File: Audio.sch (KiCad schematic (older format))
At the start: 35 parts, among them J1 AUDIO JACK, J2 AUDIO JACK, J3 AUDIO JACK, J4 AUDIO JACK, U10 TLV320AIC3104

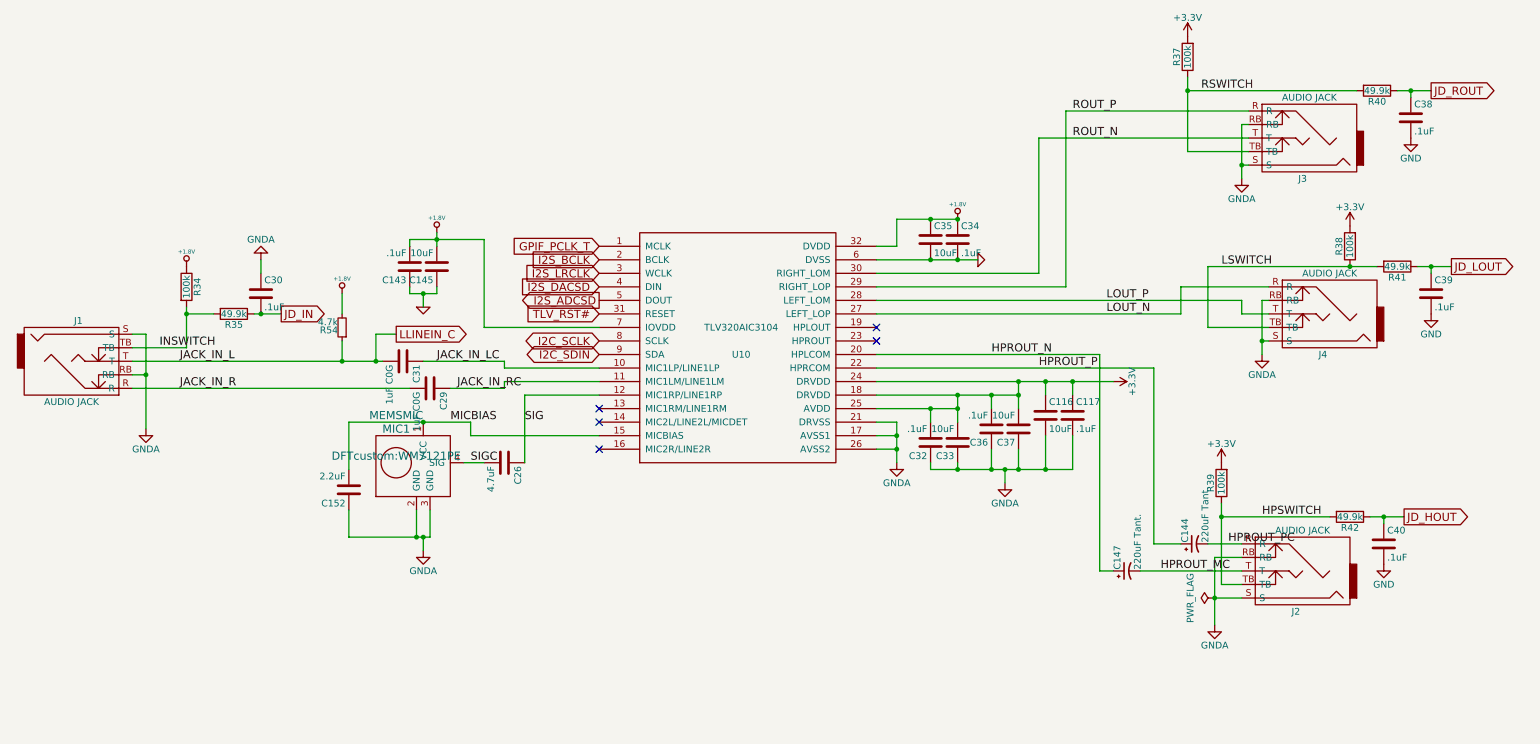
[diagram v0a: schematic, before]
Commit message: encoders and headphone jack have been modified. many unconnections
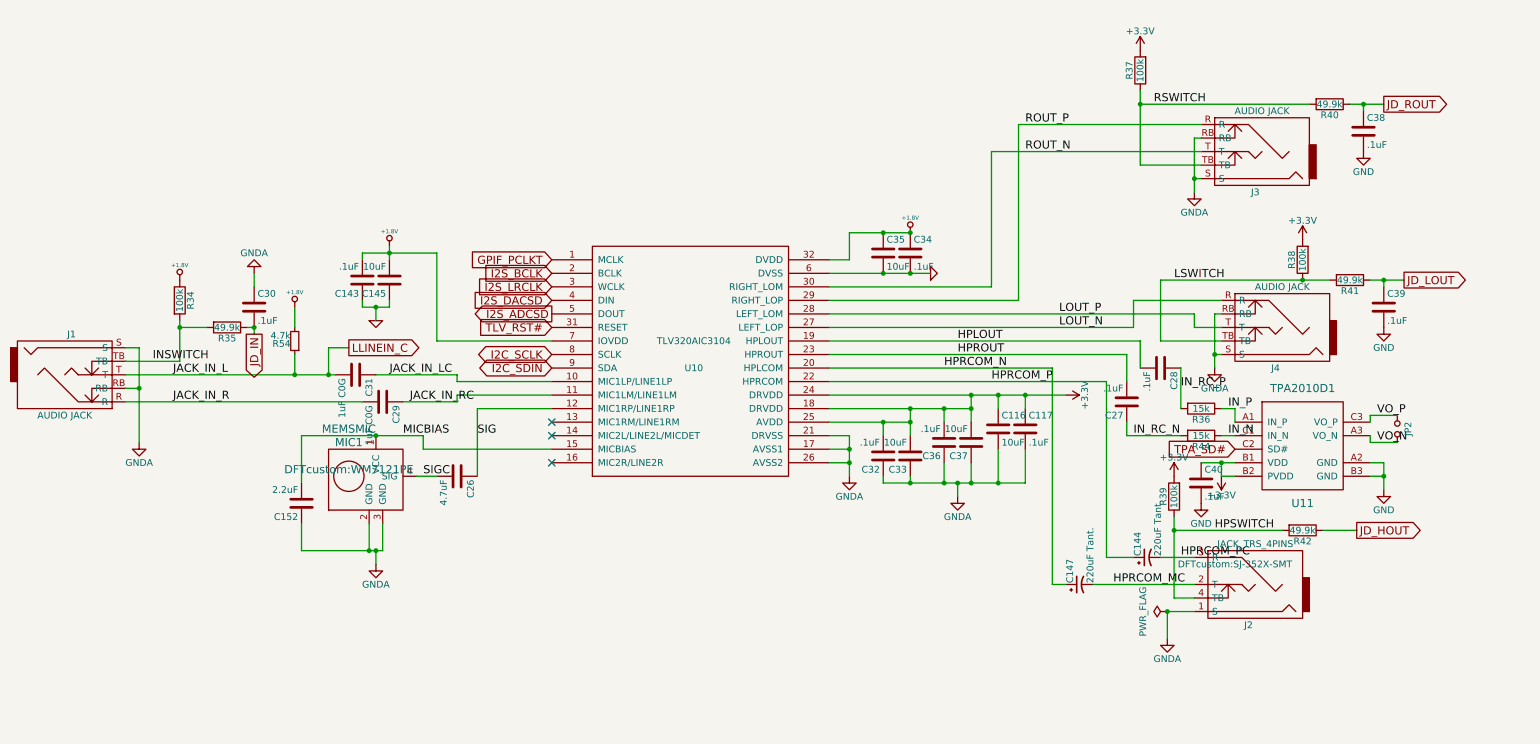
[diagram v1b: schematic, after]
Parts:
- removed J2: AUDIO JACK, DFTcustom:RA49C14B, symbol JACK_TRS_5PINS
- added C27, C28: .1uF, Capacitors_SMD:C_0603, symbol C
- added J2: JACK_TRS_4PINS, DFTcustom:SJ-352X-SMT, symbol JACK_TRS_4PINS
- added JP2: Jumper_NO_Small, DFTcustom:JUMPER_2PIN, symbol Jumper_NO_Small
- added R36, R44: 15k, Resistors_SMD:R_0402, symbol R
- added U11: TPA2010D1, DFTcustom:9DSBGA, symbol TPA2010D1
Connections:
- net +3V3: now also C40.1, U11.B1 (VDD), U11.B2 (PVDD)
- net GND: now also U11.A2 (GND), U11.B3 (GND)
- net GNDA: now also J2.1 (S)
- net HPSWITCH: now also J2.4 (TB)
- net JD_HOUT: no longer C40.1
- net HPLOUT: now reaches U10.19 (HPLOUT)
- net HPLOUT: now also C28.2
- net HPROUT: now reaches U10.23 (HPROUT)
- net HPROUT: now also C27.2
- net GPIF_PCLK_T renamed GPIF_PCLKT
- net HPROUT_MC renamed HPRCOM_MC
- net HPRCOM_MC: now also J2.2 (T)
- net HPROUT_N renamed HPRCOM_N
- net HPROUT_P renamed HPRCOM_P
- net HPROUT_PC renamed HPRCOM_PC
- net HPRCOM_PC: now also J2.3 (R)
- new net IN_N: R44.1, U11.C1 (IN_N)
- new net IN_P: R36.1, U11.A1 (IN_P)
- new net IN_RC_N: C27.1, R44.2
- new net IN_RC_P: C28.1, R36.2
- new net TPA_SD#: U11.C2 (SD#)
- new net VO_N: JP2.2, U11.A3 (VO_N)
- new net VO_P: JP2.1, U11.C3 (VO_P)
- no-connect marks 5 -> 3
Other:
- moved on the sheet: C116, C117, C143, C144, C145, C147, C152, C26, C29, C30, C31, C32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

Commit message: screen attached!
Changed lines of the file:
@@
 $Descr A4 11693 8268
 encoding utf-8
-Sheet 8 15
+Sheet 8 14
 Title ""
 Date ""
@@
 Text GLabel 4600 3300 0    60   Input ~ 0
 I2S_BCLK
-Text GLabel 4600 3600 0    60   Output ~ 0
+Text GLabel 4600 3600 0    60   BiDi ~ 0
 I2S_ADCSD
 Text GLabel 4600 3500 0    60   Input ~ 0
@@
 $EndComp
 $Comp
-L GND #PWR078
+L GND #PWR071
 U 1 1 5863064B
 P 10600 2400
-F 0 "#PWR078" H 10600 2150 50  0001 C CNN
+F 0 "#PWR071" H 10600 2150 50  0001 C CNN
 F 1 "GND" H 10600 2250 50  0000 C CNN
 F 2 "" H 10600 2400 50  0000 C CNN
@@
 $EndComp
 $Comp
-L GND #PWR079
+L GND #PWR072
 U 1 1 58630693
 P 10750 3700
-F 0 "#PWR079" H 10750 3450 50  0001 C CNN
+F 0 "#PWR072" H 10750 3450 50  0001 C CNN
 F 1 "GND" H 10750 3550 50  0000 C CNN
 F 2 "" H 10750 3700 50  0000 C CNN
@@
 $EndComp
 $Comp
-L GND #PWR080
+L GND #PWR073
 U 1 1 586306DB
 P 9400 5000
-F 0 "#PWR080" H 9400 4750 50  0001 C CNN
+F 0 "#PWR073" H 9400 4750 50  0001 C CNN
 F 1 "GND" H 9400 4850 50  0000 C CNN
 F 2 "" H 9400 5000 50  0000 C CNN
@@
 JD_HOUT
 $Comp
-L +1.8V #PWR081
+L +1.8V #PWR074
 U 1 1 58631585
 P 1850 3350
-F 0 "#PWR081" H 1850 3490 20  0001 C CNN
+F 0 "#PWR074" H 1850 3490 20  0001 C CNN
 F 1 "+1.8V" H 1850 3460 30  0000 C CNN
 F 2 "" H 1850 3350 60  0001 C CNN
@@
 JD_IN
 $Comp
-L +3.3V #PWR082
+L +3.3V #PWR075
 U 1 1 5874382A
 P 8950 1650
-F 0 "#PWR082" H 8950 1500 50  0001 C CNN
+F 0 "#PWR075" H 8950 1500 50  0001 C CNN
 F 1 "+3.3V" H 8950 1790 50  0000 C CNN
 F 2 "" H 8950 1650 50  0000 C CNN
@@
 	1550 3850 1550 4550
 $Comp
-L GNDA #PWR083
+L GNDA #PWR076
 U 1 1 58783406
 P 1550 4550
-F 0 "#PWR083" H 1550 4300 50  0001 C CNN
+F 0 "#PWR076" H 1550 4300 50  0001 C CNN
 F 1 "GNDA" H 1550 4400 50  0000 C CNN
 F 2 "" H 1550 4550 50  0000 C CNN
@@
 SIGC
 $Comp
-L GNDA #PWR084
+L GNDA #PWR077
 U 1 1 588330FF
 P 9150 6000
-F 0 "#PWR084" H 9150 5750 50  0001 C CNN
+F 0 "#PWR077" H 9150 5750 50  0001 C CNN
 F 1 "GNDA" H 9150 5850 50  0000 C CNN
 F 2 "" H 9150 6000 50  0000 C CNN
@@
 	2400 3400 2400 3300
 $Comp
-L GNDA #PWR085
+L GNDA #PWR078
 U 1 1 588CE05D
 P 2400 3300
-F 0 "#PWR085" H 2400 3050 50  0001 C CNN
+F 0 "#PWR078" H 2400 3050 50  0001 C CNN
 F 1 "GNDA" H 2400 3150 50  0000 C CNN
 F 2 "" H 2400 3300 50  0000 C CNN
@@
 $EndComp
 $Comp
-L GNDA #PWR086
+L GNDA #PWR079
 U 1 1 588D68E8
 P 6800 4800
-F 0 "#PWR086" H 6800 4550 50  0001 C CNN
+F 0 "#PWR079" H 6800 4550 50  0001 C CNN
 F 1 "GNDA" H 6800 4650 50  0000 C CNN
 F 2 "" H 6800 4800 50  0000 C CNN
@@
 Connection ~ 7050 3300
 $Comp
-L GND-RESCUE-DFTBoard #PWR087
+L GND-RESCUE-DFTBoard #PWR080
 U 1 1 588DB106
 P 7400 3300
-F 0 "#PWR087" H 7400 3300 30  0001 C CNN
+F 0 "#PWR080" H 7400 3300 30  0001 C CNN
 F 1 "GND" H 7400 3230 30  0001 C CNN
 F 2 "" H 7400 3300 60  0001 C CNN
@@
 	7250 4850 7250 4800
 $Comp
-L GNDA #PWR088
+L GNDA #PWR081
 U 1 1 588E1634
 P 3300 5450
-F 0 "#PWR088" H 3300 5200 50  0001 C CNN
+F 0 "#PWR081" H 3300 5200 50  0001 C CNN
 F 1 "GNDA" H 3300 5300 50  0000 C CNN
 F 2 "" H 3300 5450 50  0000 C CNN
@@
 	7700 4700 7700 4850
 $Comp
-L GNDA #PWR089
+L GNDA #PWR082
 U 1 1 588E39E3
 P 7600 4950
-F 0 "#PWR089" H 7600 4700 50  0001 C CNN
+F 0 "#PWR082" H 7600 4700 50  0001 C CNN
 F 1 "GNDA" H 7600 4800 50  0000 C CNN
 F 2 "" H 7600 4950 50  0000 C CNN
@@
 	3400 3550 3400 3500
 $Comp
-L GND-RESCUE-DFTBoard #PWR090
+L GND-RESCUE-DFTBoard #PWR083
 U 1 1 588BFE8C
 P 3300 3650
-F 0 "#PWR090" H 3300 3650 30  0001 C CNN
+F 0 "#PWR083" H 3300 3650 30  0001 C CNN
 F 1 "GND" H 3300 3580 30  0001 C CNN
 F 2 "" H 3300 3650 60  0001 C CNN
@@
 	9350 2600 9400 2600
 $Comp
-L GNDA #PWR091
+L GNDA #PWR084
 U 1 1 588C4253
 P 9350 2700
-F 0 "#PWR091" H 9350 2450 50  0001 C CNN
+F 0 "#PWR084" H 9350 2450 50  0001 C CNN
 F 1 "GNDA" H 9350 2550 50  0000 C CNN
 F 2 "" H 9350 2700 50  0000 C CNN
@@
 	9200 5200 10000 5200
 $Comp
-L +3.3V #PWR092
+L +3.3V #PWR085
 U 1 1 588C7336
 P 9200 4800
-F 0 "#PWR092" H 9200 4650 50  0001 C CNN
+F 0 "#PWR085" H 9200 4650 50  0001 C CNN
 F 1 "+3.3V" H 9200 4940 50  0000 C CNN
 F 2 "" H 9200 4800 50  0000 C CNN
@@
 $EndComp
 $Comp
-L +3.3V #PWR093
+L +3.3V #PWR086
 U 1 1 588C875E
 P 10150 3050
-F 0 "#PWR093" H 10150 2900 50  0001 C CNN
+F 0 "#PWR086" H 10150 2900 50  0001 C CNN
 F 1 "+3.3V" H 10150 3190 50  0000 C CNN
 F 2 "" H 10150 3050 50  0000 C CNN
@@
 $EndComp
 $Comp
-L GNDA #PWR094
+L GNDA #PWR087
 U 1 1 588CAA9F
 P 9500 4000
-F 0 "#PWR094" H 9500 3750 50  0001 C CNN
+F 0 "#PWR087" H 9500 3750 50  0001 C CNN
 F 1 "GNDA" H 9500 3850 50  0000 C CNN
 F 2 "" H 9500 4000 50  0000 C CNN
@@
 	2750 5150 2750 5350
 $Comp
-L +1.8V #PWR095
+L +1.8V #PWR088
 U 1 1 58AC439D
 P 2700 3550
-F 0 "#PWR095" H 2700 3690 20  0001 C CNN
+F 0 "#PWR088" H 2700 3690 20  0001 C CNN
 F 1 "+1.8V" H 2700 3660 30  0000 C CNN
 F 2 "" H 2700 3550 60  0001 C CNN
@@
 $EndComp
 $Comp
-L +1.8V #PWR096
+L +1.8V #PWR089
 U 1 1 58DB350D
 P 3400 3100
-F 0 "#PWR096" H 3400 3240 20  0001 C CNN
+F 0 "#PWR089" H 3400 3240 20  0001 C CNN
 F 1 "+1.8V" H 3400 3210 30  0000 C CNN
 F 2 "" H 3400 3100 60  0001 C CNN
@@
 Connection ~ 7250 3300
 $Comp
-L +1.8V #PWR097
+L +1.8V #PWR090
 U 1 1 59853AA6
 P 7250 3000
-F 0 "#PWR097" H 7250 3140 20  0001 C CNN
+F 0 "#PWR090" H 7250 3140 20  0001 C CNN
 F 1 "+1.8V" H 7250 3110 30  0000 C CNN
 F 2 "" H 7250 3000 60  0001 C CNN
@@
 Connection ~ 8100 4200
 $Comp
-L +3.3V #PWR098
+L +3.3V #PWR091
 U 1 1 59872299
 P 8400 4200
-F 0 "#PWR098" H 8400 4050 50  0001 C CNN
+F 0 "#PWR091" H 8400 4050 50  0001 C CNN
 F 1 "+3.3V" H 8400 4340 50  0000 C CNN
 F 2 "" H 8400 4200 50  0000 C CNN
@@
 $EndComp
 $Comp
-L PWR_FLAG #FLG099
+L PWR_FLAG #FLG092
 U 1 1 59875AC4
 P 9150 5800
-F 0 "#FLG099" H 9150 5895 50  0001 C CNN
+F 0 "#FLG092" H 9150 5895 50  0001 C CNN
 F 1 "PWR_FLAG" H 9150 5980 50  0000 C CNN
 F 2 "" H 9150 5800 50  0000 C CNN
@@
 Connection ~ 9550 4700
 $Comp
-L GND #PWR0100
+L GND #PWR093
 U 1 1 5982E113
 P 10750 4900
-F 0 "#PWR0100" H 10750 4650 50  0001 C CNN
+F 0 "#PWR093" H 10750 4650 50  0001 C CNN
 F 1 "GND" H 10750 4750 50  0000 C CNN
 F 2 "" H 10750 4900 50  0000 C CNN
@@
 HPROUT
 $Comp
-L +3.3V #PWR0101
+L +3.3V #PWR094
 U 1 1 5983A540
 P 9550 4800
-F 0 "#PWR0101" H 9550 4650 50  0001 C CNN
+F 0 "#PWR094" H 9550 4650 50  0001 C CNN
 F 1 "+3.3V" H 9550 4940 50  0000 C CNN
 F 2 "" H 9550 4800 50  0000 C CNN

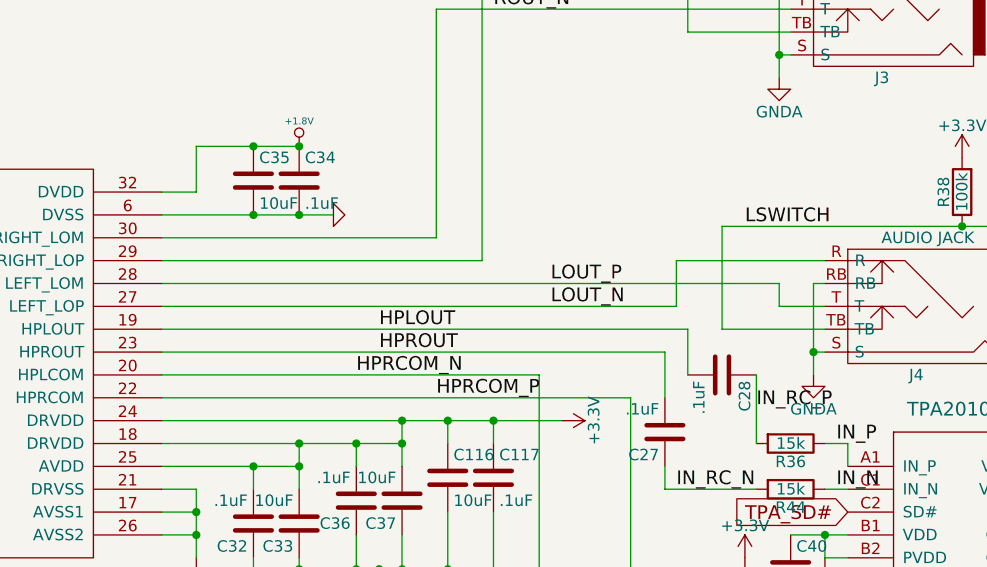
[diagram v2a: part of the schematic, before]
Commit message: just need to do the BOM before sending HW2 to PCBWAY
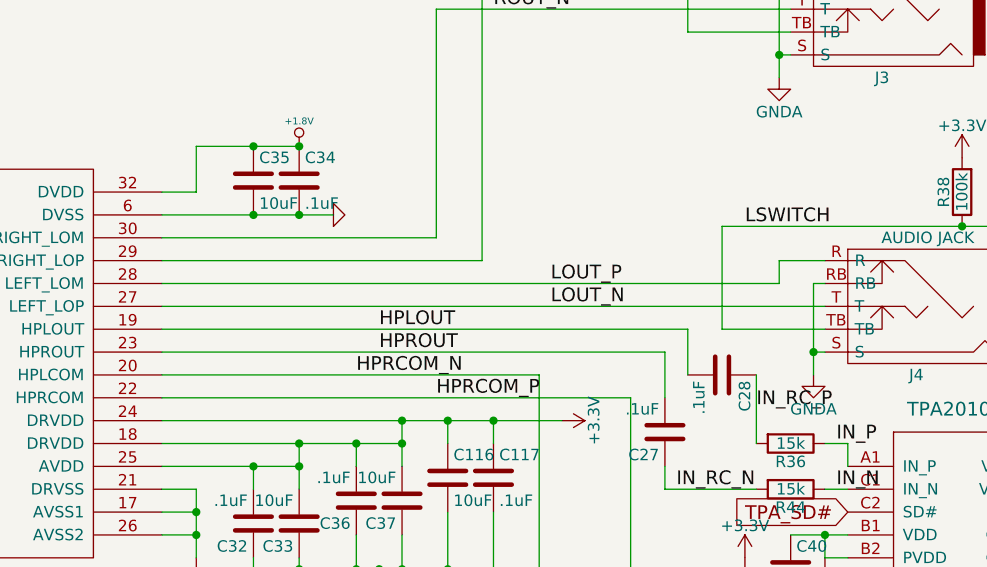
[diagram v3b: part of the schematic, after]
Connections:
- net LOUT_N: now also J4.T; no longer J4.R
- net LOUT_P: now also J4.R; no longer J4.T
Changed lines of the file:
@@
 	6650 3600 9350 3600
 Wire Wire Line
-	9350 3600 9350 3700
-Wire Wire Line
-	9350 3700 9550 3700
-Wire Wire Line
-	6650 3700 8900 3700
-Wire Wire Line
-	8900 3700 8900 3500
-Wire Wire Line
-	8900 3500 9550 3500
+	6650 3700 9550 3700
 $Comp
 L TPA2010D1 U11
@@
 Wire Wire Line
 	9150 5800 9150 6000
+Wire Wire Line
+	9550 3500 9350 3500
+Wire Wire Line
+	9350 3500 9350 3600
 $EndSCHEMATC

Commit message: using BOMs AWAY to create BOM
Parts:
- C116, C145, C33, C35, C37: MFR (none) -> Murata; MPN (none) -> GRM21BR61A106KE19L
- C117, C143, C27, C28, C30, C32, C34, C36, C38, C39, C40: MFR (none) -> Murata; MPN (none) -> GRM188R71C104KA01D
- C144, C147: MFR (none) -> AVX Corporation; MPN (none) -> F930G227KBA
- C152: MFR (none) -> Murata; MPN (none) -> GRM155R61A225KE95D
- C26: MFR (none) -> Murata; MPN (none) -> GRM21BR61A475KA73L
- J1, J3, J4: MFR (none) -> Switchcraft Conxall; MPN (none) -> RA49C12B
- MIC1: MFR (none) -> Cirrus Logic; MPN (none) -> WM7121PIMSE/RV
- R34, R37, R38, R39: MFR (none) -> Vishay Dale; MPN (none) -> CRCW0603100KFKEA
- R35, R40, R41, R42: MFR (none) -> Vishay Dale; MPN (none) -> CRCW040249K9FKED
- R54: MFR (none) -> Vishay Dale; MPN (none) -> CRCW04024K70FKED
